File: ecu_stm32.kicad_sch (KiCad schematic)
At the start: 46 parts, among them J3 ARM Cortex Debug, Y2 16MHz

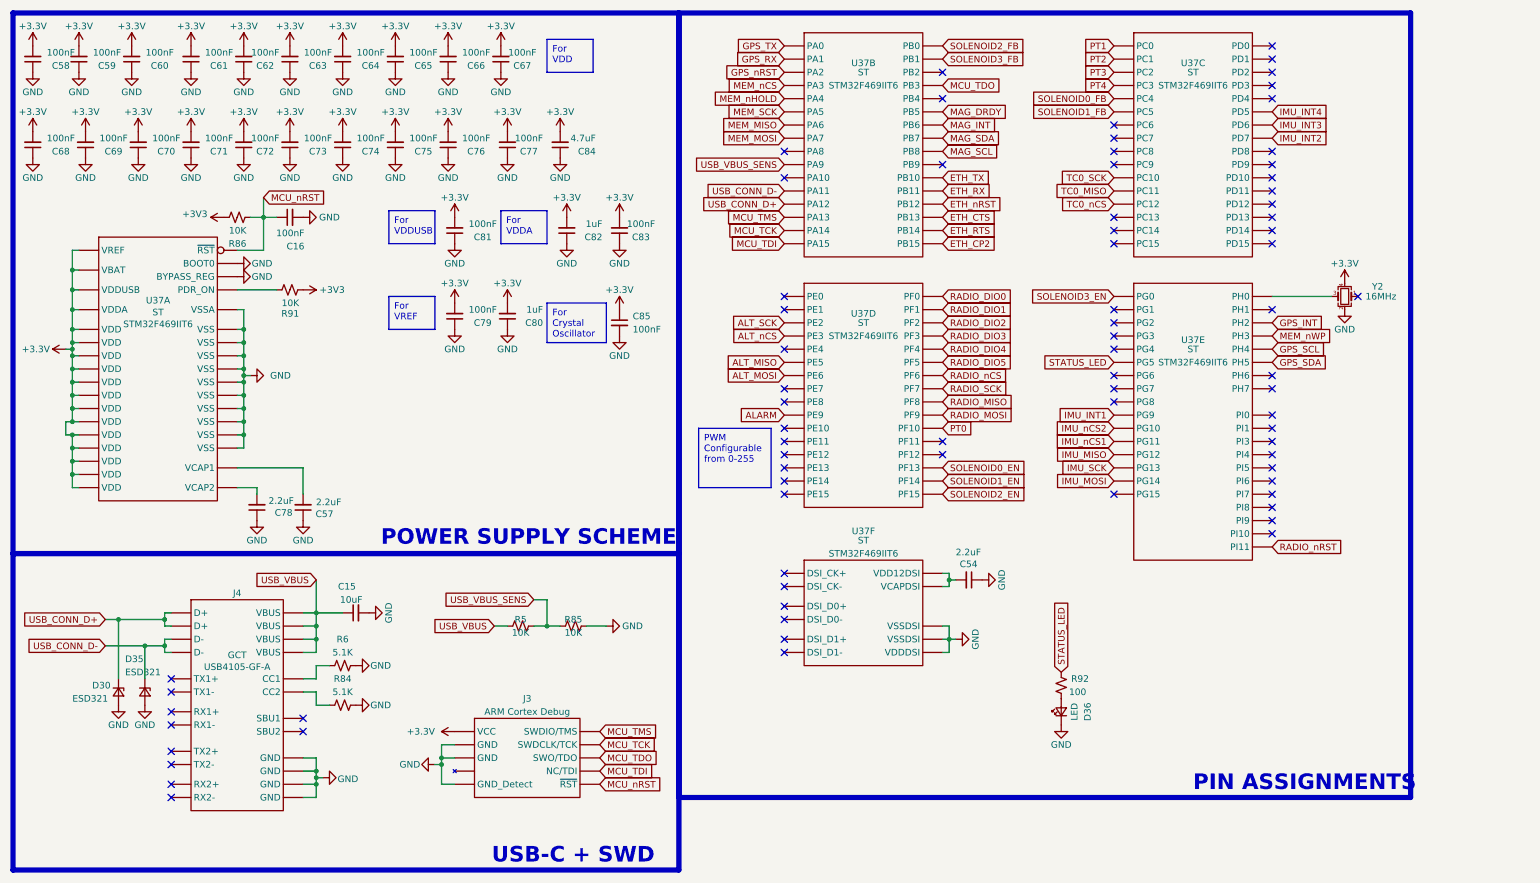
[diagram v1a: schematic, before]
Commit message: 8.02 Update; Also changed VRMs and added some notes
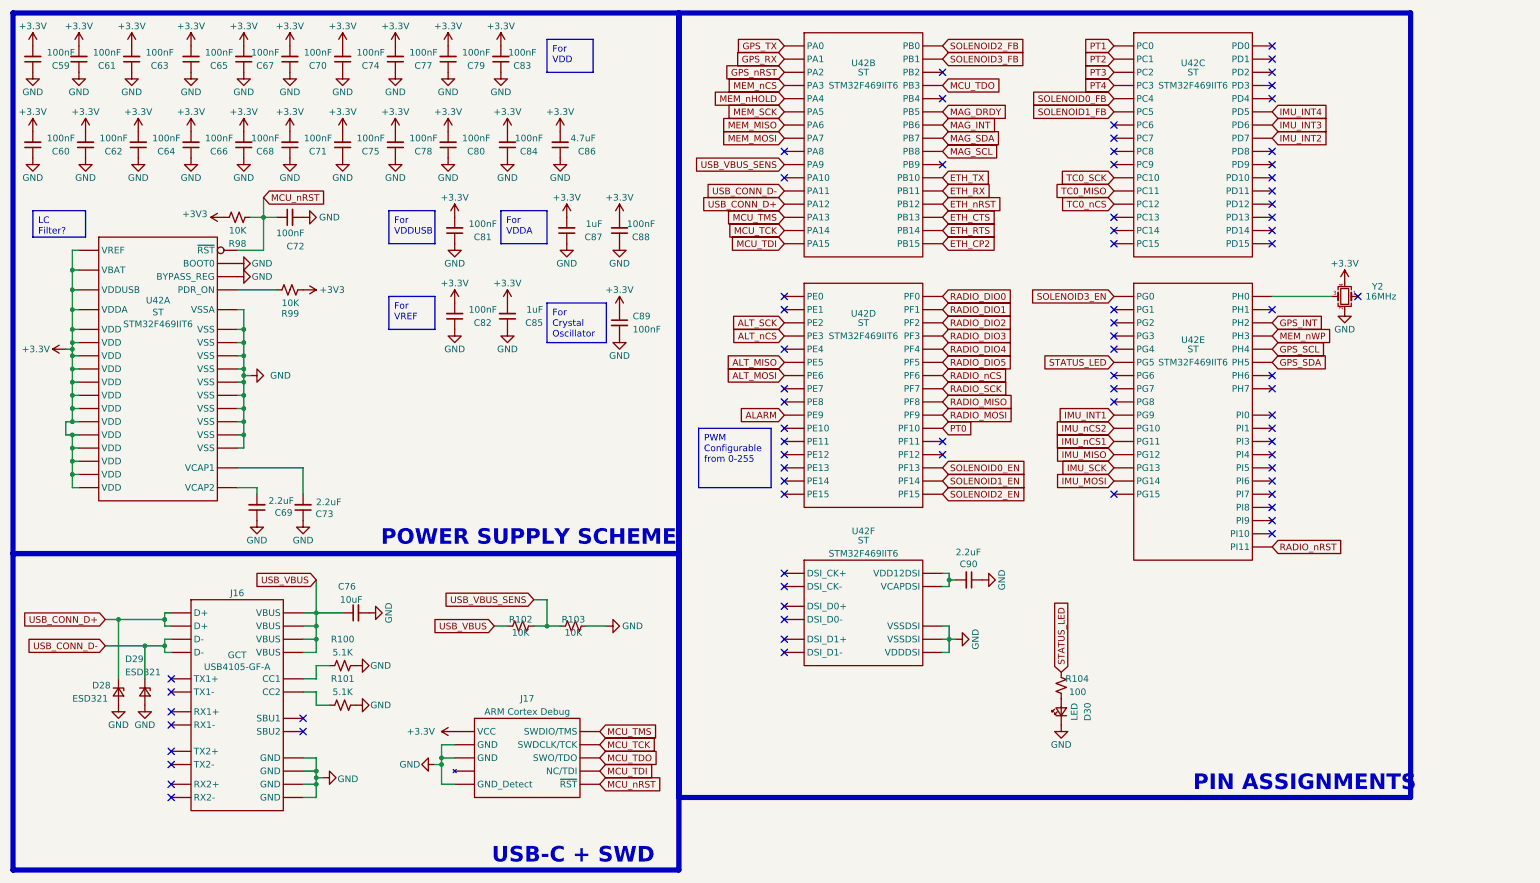
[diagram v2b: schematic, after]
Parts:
- renumbered C58 to C59, C68 to C60, C59 to C61, C69 to C62, C60 to C63, C70 to C64, C61 to C65, C71 to C66, C62 to C67, C72 to C68, C78 to C69, C63 to C70, C73 to C71, C16 to C72, C57 to C73, C64 to C74, C74 to C75, C15 to C76, C65 to C77, C75 to C78, C66 to C79, C76 to C80, C79 to C82, C67 to C83, C77 to C84, C80 to C85, C84 to C86, C82 to C87, C83 to C88, C85 to C89, C54 to C90, D30 to D28, D35 to D29, D36 to D30, J4 to J16, J3 to J17, R6 to R100, R84 to R101, R5 to R102, R85 to R103, R92 to R104, R86 to R98, R91 to R99, U37 to U42

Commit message: ECU essentially reviewable
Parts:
- renumbered D28 to D35, D29 to D36, D30 to D37, R98 to R103, R99 to R104, R100 to R105, R101 to R106, R102 to R107, R103 to R108, R104 to R109, U42 to U40
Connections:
- net MEM_nHOLD renamed MEM1_nCS
- net MEM_nWP renamed UNUSED_GPIO
- net RADIO_DIO2 renamed RADIO1_DIO0
- net RADIO_DIO3 renamed RADIO1_DIO1
- net RADIO_DIO4 renamed RADIO1_nCS
- net RADIO_DIO5 renamed RADIO1_nRST
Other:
- moved on the sheet: Y2

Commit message: addressed PR comments
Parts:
- renumbered D35 to D34, D36 to D35, D37 to D36
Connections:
- net GPS_nRST is gone; now on net UNUSED_GPIO: U40.42 (PA2)

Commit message: Updated schematic with IOC
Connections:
- net GPS_INT: now also U40.42 (PA2); no longer U40.43 (PH2)
- net RADIO2_nCS: now reaches U40.10 (PC15)
- net TC1_nCS: now reaches U40.142 (PD0)
- net RADIO2_nRST: now reaches U40.9 (PC14)
- net RADIO2_DIO0: now reaches U40.11 (PI9)
- net RADIO2_DIO1: now reaches U40.12 (PI10)
- net UNUSED_GPIO renamed PT6
- net PT6: no longer U40.42 (PA2)
- new net PT5: U40.43 (PH2)
- no-connect marks 76 -> 71
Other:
- note added: "NOTE THESE ARE ON ANALOG PINS NOT ADC (idk how much this matters)"
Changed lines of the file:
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@@
 	)
 	(no_connect
-		(at 256.54 114.3)
-	)
-	(no_connect
 		(at 44.45 158.75)
 	)
@@
 	)
 	(no_connect
-		(at 226.06 58.42)
-	)
-	(no_connect
 		(at 226.06 43.18)
 	)
@@
 	)
 	(no_connect
-		(at 256.54 20.32)
-	)
-	(no_connect
 		(at 162.56 96.52)
 	)
@@
 	)
 	(no_connect
-		(at 256.54 111.76)
-	)
-	(no_connect
 		(at 226.06 35.56)
 	)
@@
 	)
 	(no_connect
-		(at 226.06 55.88)
-	)
-	(no_connect
 		(at 226.06 76.2)
 	)
@@
 		)
 	)
+	(text "NOTE THESE ARE ON ANALOG PINS\nNOT ADC (idk how much this matters)"
+		(exclude_from_sim no)
+		(at 283.972 74.93 0)
+		(effects
+			(font
+				(size 1.27 1.27)
+				(color 255 39 10 1)
+			)
+		)
+	)
 	(text "USB-C + SWD"
 		(exclude_from_sim no)
@@
 		)
 	)
+	(global_label "PT5"
+		(shape input)
+		(at 256.54 73.66 0)
+		(fields_autoplaced yes)
+		(effects
+			(font
+				(size 1.27 1.27)
+			)
+			(justify left)
+		)
+		(property "Intersheetrefs" "${INTERSHEET_REFS}"
+			(at 262.9723 73.66 0)
+			(effects
+				(font
+					(size 1.27 1.27)
+				)
+				(justify left)
+				(hide yes)
+			)
+		)
+	)
 	(global_label "USB_VBUS"
 		(shape input)
@@
 		)
 	)
+	(global_label "RADIO2_DIO1"
+		(shape input)
+		(at 256.54 114.3 0)
+		(fields_autoplaced yes)
+		(effects
+			(font
+				(size 1.27 1.27)
+			)
+			(justify left)
+		)
+		(property "Intersheetrefs" "${INTERSHEET_REFS}"
+			(at 271.681 114.3 0)
+			(effects
+				(font
+					(size 1.27 1.27)
+				)
+				(justify left)
+				(hide yes)
+			)
+		)
+	)
 	(global_label "MCU_nRST"
 		(shape input)
@@
 		)
 	)
-	(global_label "UNUSED_GPIO"
-		(shape input)
-		(at 256.54 76.2 0)
-		(fields_autoplaced yes)
-		(effects
-			(font
-				(size 1.27 1.27)
-				(color 255 10 19 1)
-			)
-			(justify left)
-		)
-		(property "Intersheetrefs" "${INTERSHEET_REFS}"
-			(at 272.5881 76.2 0)
-			(effects
-				(font
-					(size 1.27 1.27)
-				)
-				(justify left)
-				(hide yes)
-			)
-		)
-	)
 	(global_label "MCU_TMS"
 		(shape input)
@@
 		)
 	)
-	(global_label "UNUSED_GPIO"
+	(global_label "MAG_DRDY"
 		(shape input)
-		(at 162.56 25.4 180)
+		(at 193.04 33.02 0)
+		(fields_autoplaced yes)
+		(effects
+			(font
+				(size 1.27 1.27)
+			)
+			(justify left)
+		)
+		(property "Intersheetrefs" "${INTERSHEET_REFS}"
+			(at 205.622 33.02 0)
+			(effects
+				(font
+					(size 1.27 1.27)
+				)
+				(justify left)
+				(hide yes)
+			)
+		)
+	)
+	(global_label "RADIO2_nRST"
+		(shape input)
+		(at 226.06 55.88 180)
 		(fields_autoplaced yes)
 		(effects
 			(font
 				(size 1.27 1.27)
-				(color 255 10 19 1)
 			)
 			(justify right)
 		)
 		(property "Intersheetrefs" "${INTERSHEET_REFS}"
-			(at 146.5119 25.4 0)
+			(at 210.7377 55.88 0)
 			(effects
 				(font
@@
 		)
 	)
-	(global_label "MAG_DRDY"
+	(global_label "RADIO2_DIO0"
 		(shape input)
-		(at 193.04 33.02 0)
+		(at 256.54 111.76 0)
 		(fields_autoplaced yes)
 		(effects
@@
 		)
 		(property "Intersheetrefs" "${INTERSHEET_REFS}"
-			(at 205.622 33.02 0)
+			(at 271.681 111.76 0)
 			(effects
 				(font
@@
 		)
 	)
-	(global_label "GPS_INT"
+	(global_label "TC1_nCS"
 		(shape input)
-		(at 256.54 73.66 0)
+		(at 256.54 20.32 0)
 		(fields_autoplaced yes)
 		(effects
@@
 		)
 		(property "Intersheetrefs" "${INTERSHEET_REFS}"
-			(at 267.0658 73.66 0)
+			(at 267.5684 20.32 0)
 			(effects
 				(font
@@
 		)
 	)
+	(global_label "GPS_INT"
+		(shape input)
+		(at 162.56 25.4 180)
+		(fields_autoplaced yes)
+		(effects
+			(font
+				(size 1.27 1.27)
+			)
+			(justify right)
+		)
+		(property "Intersheetrefs" "${INTERSHEET_REFS}"
+			(at 151.9548 25.4 0)
+			(effects
+				(font
+					(size 1.27 1.27)
+				)
+				(justify right)
+				(hide yes)
+			)
+		)
+	)
+	(global_label "RADIO2_nCS"
+		(shape input)
+		(at 226.06 58.42 180)
+		(fields_autoplaced yes)
+		(effects
+			(font
+				(size 1.27 1.27)
+			)
+			(justify right)
+		)
+		(property "Intersheetrefs" "${INTERSHEET_REFS}"
+			(at 211.7053 58.42 0)
+			(effects
+				(font
+					(size 1.27 1.27)
+				)
+				(justify right)
+				(hide yes)
+			)
+		)
+	)
 	(global_label "SOLENOID2_FB"
 		(shape input)
@@
 			(effects
 				(font
+					(size 1.27 1.27)
+				)
+				(justify left)
+				(hide yes)
+			)
+		)
+	)
+	(global_label "PT6"
+		(shape input)
+		(at 256.54 76.2 0)
+		(fields_autoplaced yes)
+		(effects
+			(font
+				(size 1.27 1.27)
+			)
+			(justify left)
+		)
+		(property "Intersheetrefs" "${INTERSHEET_REFS}"
+			(at 262.9723 76.2 0)
+			(effects
+				(font

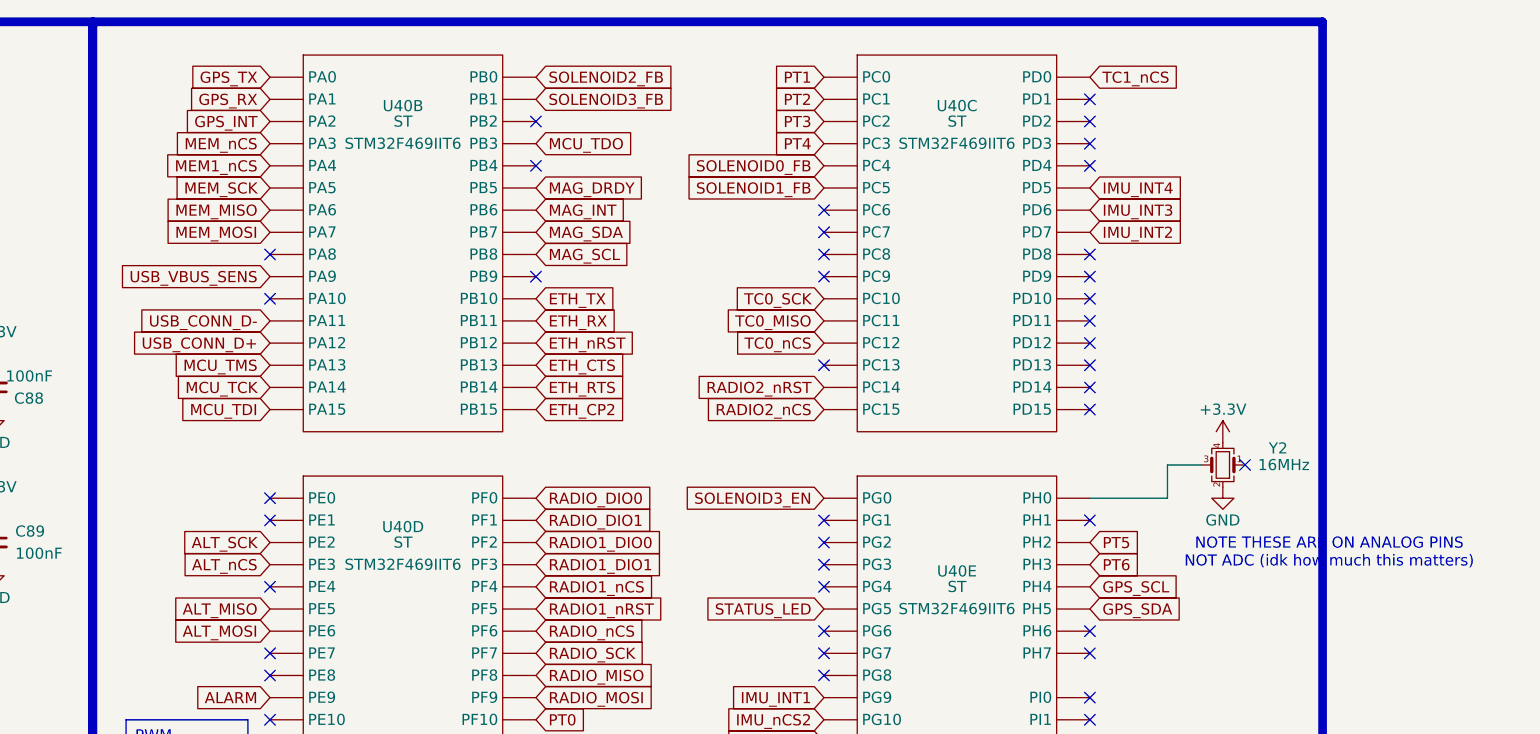
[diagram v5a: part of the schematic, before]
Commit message: Moved PTs to ADC pins
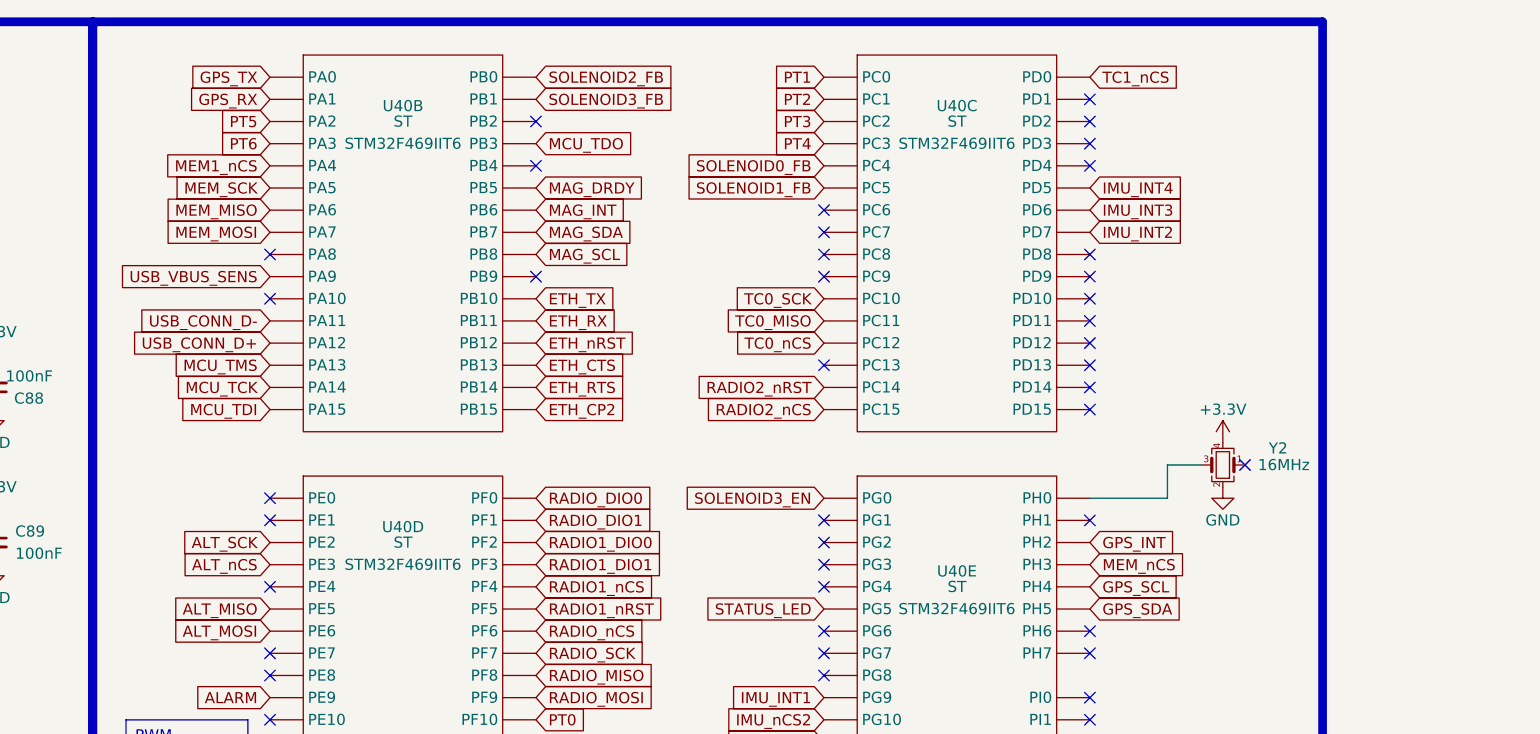
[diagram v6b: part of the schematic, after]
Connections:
- net GPS_INT: now also U40.43 (PH2); no longer U40.42 (PA2)
- net MEM_nCS: now also U40.44 (PH3); no longer U40.47 (PA3)
- net PT5: now also U40.42 (PA2); no longer U40.43 (PH2)
- net PT6: now also U40.47 (PA3); no longer U40.44 (PH3)
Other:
- note removed: "NOTE THESE ARE ON ANALOG PINS NOT ADC (idk how much this matters)"

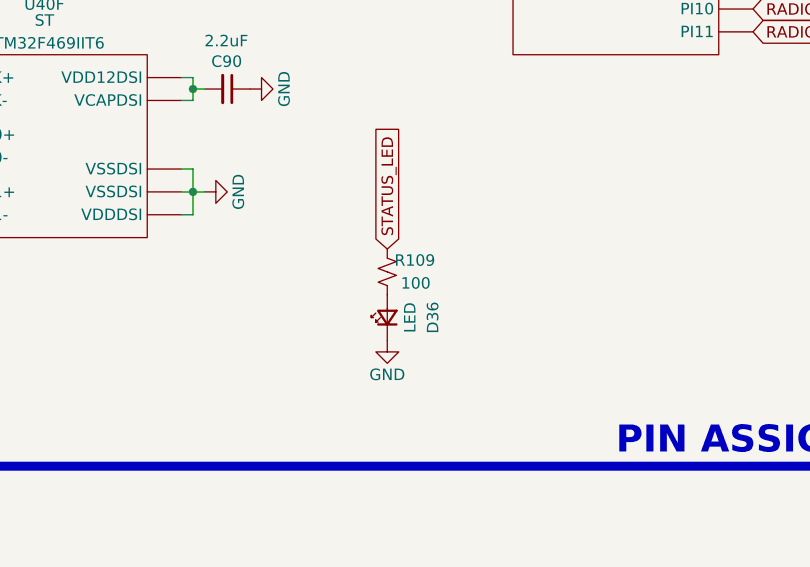
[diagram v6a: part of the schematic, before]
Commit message: Assigned almost all footprints
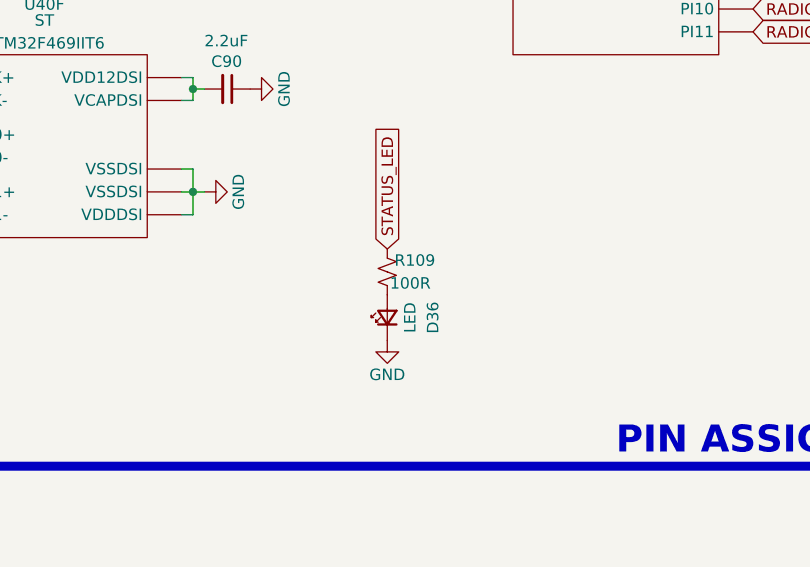
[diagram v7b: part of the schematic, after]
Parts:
- C59, C60, C61, C62, C63, C64, C65, C66, C67, C68, C70, C71, C74, C75, C77, C78, C79, C80, C81, C82, C83, C84, C88: footprint Capacitor_SMD:C_0603_1608Metric -> Capacitor_SMD:C_0402_1005Metric; Part # Generic 0603 100nF 6.3V X7R MLCC -> Generic 100nF 6.3V X7R 0402 MLCC
- C72: footprint Capacitor_SMD:C_0603_1608Metric_Pad1.08x0.95mm_HandSolder -> Capacitor_SMD:C_0402_1005Metric; Part # Generic 0603 100nF 6.3V X7R MLCC -> Generic 100nF 6.3V X7R 0402 MLCC
- D36: footprint Diode_SMD:D_0603_1608Metric_Pad1.05x0.95mm_HandSolder -> LED_SMD:LED_0603_1608Metric_Pad1.05x0.95mm_HandSolder
- R103, R104, R107, R108: footprint Resistor_SMD:R_0603_1608Metric_Pad0.98x0.95mm_HandSolder -> Resistor_SMD:R_0402_1005Metric; Part # Generic 0603 10K 1% Resistor -> Generic 10K 1% 0402 Resistor
- R109: value 100 -> 100R; footprint Resistor_SMD:R_0603_1608Metric_Pad0.98x0.95mm_HandSolder -> Resistor_SMD:R_0402_1005Metric; Part # Generic 0603 100 1% Resistor -> Generic 100R 1% 0402 Resistor

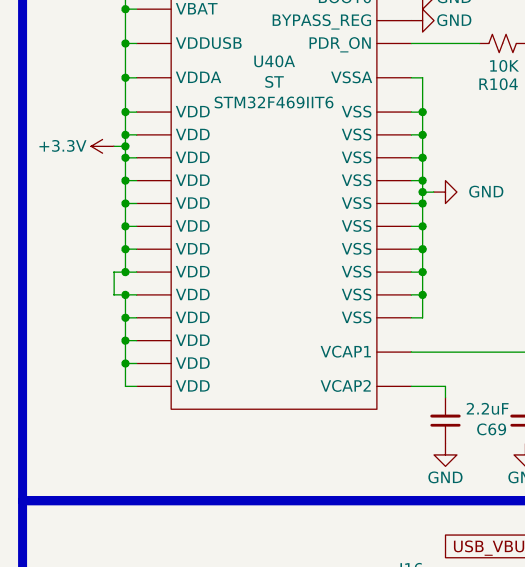
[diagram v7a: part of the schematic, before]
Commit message: Replaced Regs
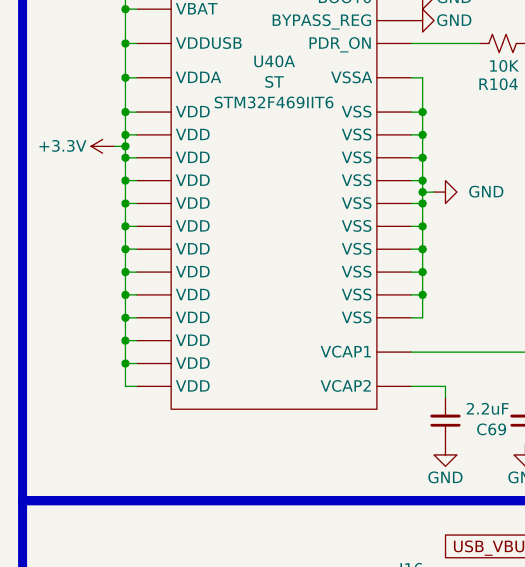
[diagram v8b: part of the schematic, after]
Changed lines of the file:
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@@
-	(wire
-		(pts
-			(xy 24.13 92.71) (xy 25.4 92.71)
-		)
-		(stroke
-			(width 0)
-			(type default)
-		)
-	)
 	(wire
 		(pts
@@
 	(wire
 		(pts
-			(xy 24.13 95.25) (xy 25.4 95.25)
-		)
-		(stroke
-			(width 0)
-			(type default)
-		)
-	)
-	(wire
-		(pts
 			(xy 193.04 124.46) (xy 194.31 124.46)
 		)
@@
 	(wire
 		(pts
-			(xy 24.13 92.71) (xy 24.13 95.25)
-		)
-		(stroke
+			(xy 25.4 92.71) (xy 25.4 95.25)
+		)
+		(stroke
